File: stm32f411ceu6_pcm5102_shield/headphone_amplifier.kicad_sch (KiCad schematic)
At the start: 17 parts, among them J1 AudioJack3_Ground_SwitchTR, Q1 BC337, Q2 BC337

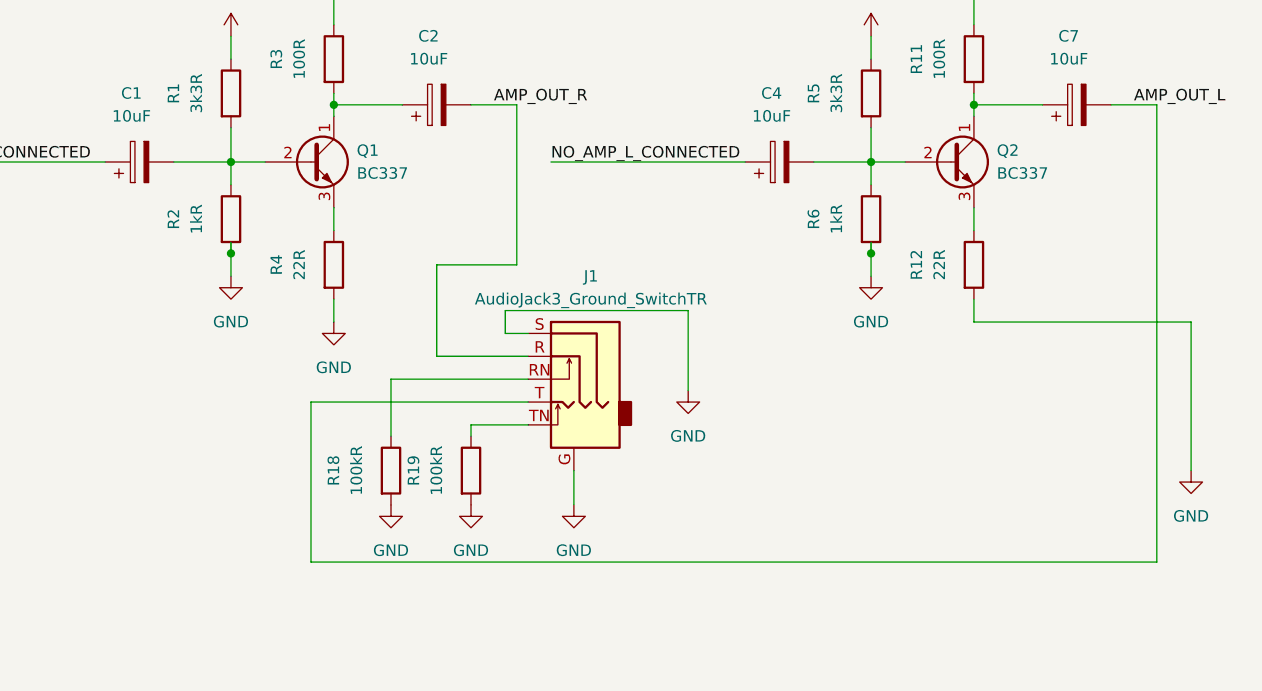
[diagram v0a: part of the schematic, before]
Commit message: Add rotary encoder
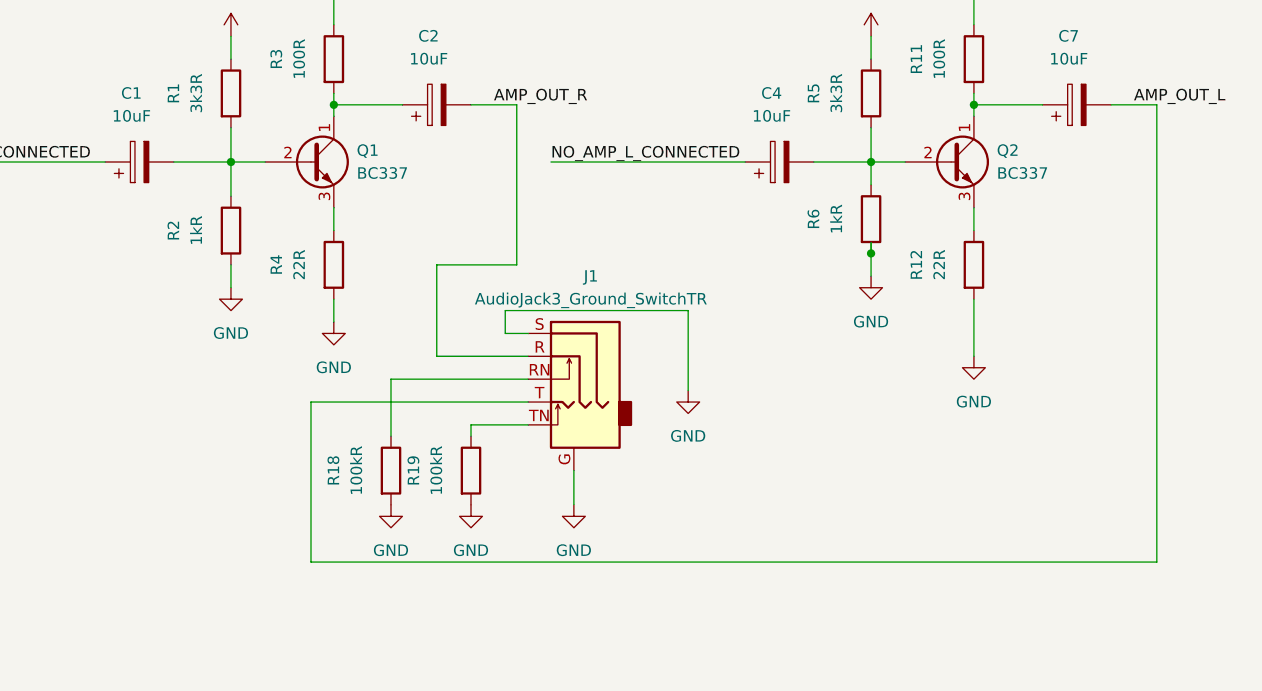
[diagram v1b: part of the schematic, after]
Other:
- moved on the sheet: R2
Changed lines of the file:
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@@
 		(color 0 0 0 0)
 	)
-	(junction
-		(at 59.69 59.69)
-		(diameter 0)
-		(color 0 0 0 0)
-	)
 	(wire
 		(pts
@@
 	(wire
 		(pts
-			(xy 59.69 49.53) (xy 59.69 52.07)
+			(xy 59.69 49.53) (xy 59.69 53.34)
 		)
 		(stroke
@@
 	(wire
 		(pts
-			(xy 142.24 64.77) (xy 142.24 67.31)
-		)
-		(stroke
-			(width 0)
-			(type default)
-		)
-	)
-	(wire
-		(pts
 			(xy 142.24 41.91) (xy 142.24 43.18)
 		)
@@
 	(wire
 		(pts
-			(xy 142.24 67.31) (xy 166.37 67.31)
+			(xy 142.24 43.18) (xy 149.86 43.18)
 		)
 		(stroke
@@
 	(wire
 		(pts
-			(xy 142.24 43.18) (xy 149.86 43.18)
+			(xy 92.71 73.66) (xy 77.47 73.66)
 		)
 		(stroke
@@
 	(wire
 		(pts
-			(xy 92.71 73.66) (xy 77.47 73.66)
+			(xy 124.46 49.53) (xy 130.81 49.53)
 		)
 		(stroke
@@
 	(wire
 		(pts
-			(xy 124.46 49.53) (xy 130.81 49.53)
+			(xy 92.71 78.74) (xy 86.36 78.74)
 		)
 		(stroke
@@
 	(wire
 		(pts
-			(xy 92.71 78.74) (xy 86.36 78.74)
+			(xy 157.48 43.18) (xy 162.56 43.18)
 		)
 		(stroke
@@
 	(wire
 		(pts
-			(xy 157.48 43.18) (xy 162.56 43.18)
+			(xy 59.69 60.96) (xy 59.69 63.5)
 		)
 		(stroke
@@
 	(wire
 		(pts
-			(xy 59.69 59.69) (xy 59.69 62.23)
-		)
-		(stroke
-			(width 0)
-			(type default)
-		)
-	)
-	(wire
-		(pts
-			(xy 166.37 67.31) (xy 166.37 83.82)
+			(xy 142.24 64.77) (xy 142.24 71.12)
 		)
 		(stroke
@@
 	(wire
 		(pts
-			(xy 59.69 58.42) (xy 59.69 59.69)
-		)
-		(stroke
-			(width 0)
-			(type default)
-		)
-	)
-	(wire
-		(pts
 			(xy 130.81 45.72) (xy 130.81 49.53)
 		)
@@
 	(symbol
 		(lib_id "power:GND")
-		(at 59.69 62.23 0)
+		(at 59.69 63.5 0)
 		(unit 1)
 		(exclude_from_sim no)
@@
 		(fields_autoplaced yes)
 		(property "Reference" "#PWR011"
-			(at 59.69 68.58 0)
+			(at 59.69 69.85 0)
 			(effects
 				(font
@@
 		)
 		(property "Value" "GND"
-			(at 59.69 67.31 0)
+			(at 59.69 68.58 0)
 			(effects
 				(font
@@
 		)
 		(property "Footprint" ""
-			(at 59.69 62.23 0)
+			(at 59.69 63.5 0)
 			(effects
 				(font
@@
 		)
 		(property "Datasheet" ""
-			(at 59.69 62.23 0)
+			(at 59.69 63.5 0)
 			(effects
 				(font
@@
 		)
 		(property "Description" "Power symbol creates a global label with name \"GND\" , ground"
-			(at 59.69 62.23 0)
+			(at 59.69 63.5 0)
 			(effects
 				(font
@@
 	(symbol
 		(lib_id "Device:R")
-		(at 59.69 55.88 0)
+		(at 59.69 57.15 0)
 		(unit 1)
 		(exclude_from_sim no)
@@
 		(dnp no)
 		(property "Reference" "R2"
-			(at 53.34 55.88 90)
+			(at 53.34 57.15 90)
 			(effects
 				(font
@@
 		)
 		(property "Value" "1kR"
-			(at 55.88 55.88 90)
+			(at 55.88 57.15 90)
 			(effects
 				(font
@@
 		)
 		(property "Footprint" "Resistor_SMD:R_0805_2012Metric"
-			(at 57.912 55.88 90)
+			(at 57.912 57.15 90)
 			(effects
 				(font
@@
 		)
 		(property "Datasheet" "~"
-			(at 59.69 55.88 0)
+			(at 59.69 57.15 0)
 			(effects
 				(font
@@
 		)
 		(property "Description" ""
-			(at 59.69 55.88 0)
+			(at 59.69 57.15 0)
 			(effects
 				(font
@@
 		)
 		(property "LCSC link" "https://www.lcsc.com/product-detail/Chip-Resistor-Surface-Mount_UNI-ROYAL-Uniroyal-Elec-0805W8F100JT5E_C17415.html"
-			(at 59.69 55.88 0)
+			(at 59.69 57.15 0)
 			(effects
 				(font
@@
 		)
 		(property "Manufacturer" "UNI-ROYAL(Uniroyal Elec)"
-			(at 59.69 55.88 0)
+			(at 59.69 57.15 0)
 			(effects
 				(font
@@
 		)
 		(property "Manufacturer Part Number" "0805W8F100JT5E"
-			(at 59.69 55.88 0)
+			(at 59.69 57.15 0)
 			(effects
 				(font
@@
 	(symbol
 		(lib_id "power:GND")
-		(at 166.37 83.82 0)
+		(at 142.24 71.12 0)
 		(unit 1)
 		(exclude_from_sim no)
@@
 		(fields_autoplaced yes)
 		(property "Reference" "#PWR023"
-			(at 166.37 90.17 0)
+			(at 142.24 77.47 0)
 			(effects
 				(font
@@
 		)
 		(property "Value" "GND"
-			(at 166.37 88.9 0)
+			(at 142.24 76.2 0)
 			(effects
 				(font
@@
 		)
 		(property "Footprint" ""
-			(at 166.37 83.82 0)
+			(at 142.24 71.12 0)
 			(effects
 				(font
@@
 		)
 		(property "Datasheet" ""
-			(at 166.37 83.82 0)
+			(at 142.24 71.12 0)
 			(effects
 				(font
@@
 		)
 		(property "Description" "Power symbol creates a global label with name \"GND\" , ground"
-			(at 166.37 83.82 0)
+			(at 142.24 71.12 0)
 			(effects
 				(font

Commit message: Items numeration fix
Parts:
- renumbered C1 to C300, C2 to C301, C4 to C302, C7 to C303, J1 to J300, Q1 to Q300, Q2 to Q301, R1 to R300, R2 to R301, R3 to R302, R4 to R303, R5 to R304, R6 to R305, R11 to R306, R12 to R307, R18 to R308, R19 to R309
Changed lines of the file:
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@@
 		(dnp no)
 		(fields_autoplaced yes)
-		(property "Reference" "C1"
+		(property "Reference" "C300"
 			(at 48.641 41.91 90)
 			(effects
@@
 			(project "stm32f411ceu6_pcm5102_shield"
 				(path "/aeaad843-2b7c-40e9-bb1d-8d1f5e5d5206/73f0023b-2db5-4e36-9906-e9384dd08abf"
-					(reference "C1")
+					(reference "C300")
 					(unit 1)
 				)
@@
 		(dnp no)
 		(fields_autoplaced yes)
-		(property "Reference" "C2"
+		(property "Reference" "C301"
 			(at 81.661 35.56 90)
 			(effects
@@
 			(project "stm32f411ceu6_pcm5102_shield"
 				(path "/aeaad843-2b7c-40e9-bb1d-8d1f5e5d5206/73f0023b-2db5-4e36-9906-e9384dd08abf"
-					(reference "C2")
+					(reference "C301")
 					(unit 1)
 				)
@@
 		(on_board yes)
 		(dnp no)
-		(property "Reference" "R11"
+		(property "Reference" "R306"
 			(at 135.89 38.1 90)
 			(effects
@@
 			(project "stm32f411ceu6_pcm5102_shield"
 				(path "/aeaad843-2b7c-40e9-bb1d-8d1f5e5d5206/73f0023b-2db5-4e36-9906-e9384dd08abf"
-					(reference "R11")
+					(reference "R306")
 					(unit 1)
 				)
@@
 		(dnp no)
 		(fields_autoplaced yes)
-		(property "Reference" "C7"
+		(property "Reference" "C303"
 			(at 152.781 35.56 90)
 			(effects
@@
 			(project "stm32f411ceu6_pcm5102_shield"
 				(path "/aeaad843-2b7c-40e9-bb1d-8d1f5e5d5206/73f0023b-2db5-4e36-9906-e9384dd08abf"
-					(reference "C7")
+					(reference "C303")
 					(unit 1)
 				)
@@
 		(on_board yes)
 		(dnp no)
-		(property "Reference" "R19"
+		(property "Reference" "R309"
 			(at 80.01 83.82 90)
 			(effects
@@
 			(project "stm32f411ceu6_pcm5102_shield"
 				(path "/aeaad843-2b7c-40e9-bb1d-8d1f5e5d5206/73f0023b-2db5-4e36-9906-e9384dd08abf"
-					(reference "R19")
+					(reference "R309")
 					(unit 1)
 				)
@@
 		(on_board yes)
 		(dnp no)
-		(property "Reference" "R18"
+		(property "Reference" "R308"
 			(at 71.12 83.82 90)
 			(effects
@@
 			(project "stm32f411ceu6_pcm5102_shield"
 				(path "/aeaad843-2b7c-40e9-bb1d-8d1f5e5d5206/73f0023b-2db5-4e36-9906-e9384dd08abf"
-					(reference "R18")
+					(reference "R308")
 					(unit 1)
 				)
@@
 		(dnp no)
 		(fields_autoplaced yes)
-		(property "Reference" "C4"
+		(property "Reference" "C302"
 			(at 119.761 41.91 90)
 			(effects
@@
 			(project "stm32f411ceu6_pcm5102_shield"
 				(path "/aeaad843-2b7c-40e9-bb1d-8d1f5e5d5206/73f0023b-2db5-4e36-9906-e9384dd08abf"
-					(reference "C4")
+					(reference "C302")
 					(unit 1)
 				)
@@
 		(on_board yes)
 		(dnp no)
-		(property "Reference" "R2"
+		(property "Reference" "R301"
 			(at 53.34 57.15 90)
 			(effects
@@
 			(project "stm32f411ceu6_pcm5102_shield"
 				(path "/aeaad843-2b7c-40e9-bb1d-8d1f5e5d5206/73f0023b-2db5-4e36-9906-e9384dd08abf"
-					(reference "R2")
+					(reference "R301")
 					(unit 1)
 				)
@@
 		(dnp no)
 		(fields_autoplaced yes)
-		(property "Reference" "Q2"
+		(property "Reference" "Q301"
 			(at 144.78 48.2599 0)
 			(effects
@@
 			(project "stm32f411ceu6_pcm5102_shield"
 				(path "/aeaad843-2b7c-40e9-bb1d-8d1f5e5d5206/73f0023b-2db5-4e36-9906-e9384dd08abf"
-					(reference "Q2")
+					(reference "Q301")
 					(unit 1)
 				)
@@
 		(on_board yes)
 		(dnp no)
-		(property "Reference" "R12"
+		(property "Reference" "R307"
 			(at 135.89 60.96 90)
 			(effects
@@
 			(project "stm32f411ceu6_pcm5102_shield"
 				(path "/aeaad843-2b7c-40e9-bb1d-8d1f5e5d5206/73f0023b-2db5-4e36-9906-e9384dd08abf"
-					(reference "R12")
+					(reference "R307")
 					(unit 1)
 				)
@@
 		(dnp no)
 		(fields_autoplaced yes)
-		(property "Reference" "J1"
+		(property "Reference" "J300"
 			(at 99.695 62.23 0)
 			(effects
@@
 			(project "stm32f411ceu6_pcm5102_shield"
 				(path "/aeaad843-2b7c-40e9-bb1d-8d1f5e5d5206/73f0023b-2db5-4e36-9906-e9384dd08abf"
-					(reference "J1")
+					(reference "J300")
 					(unit 1)
 				)
@@
 		(on_board yes)
 		(dnp no)
-		(property "Reference" "R5"
+		(property "Reference" "R304"
 			(at 124.46 41.91 90)
 			(effects
@@
 			(project "stm32f411ceu6_pcm5102_shield"
 				(path "/aeaad843-2b7c-40e9-bb1d-8d1f5e5d5206/73f0023b-2db5-4e36-9906-e9384dd08abf"
-					(reference "R5")
+					(reference "R304")
 					(unit 1)
 				)
@@
 		(on_board yes)
 		(dnp no)
-		(property "Reference" "R4"
+		(property "Reference" "R303"
 			(at 64.77 60.96 90)
 			(effects
@@
 			(project "stm32f411ceu6_pcm5102_shield"
 				(path "/aeaad843-2b7c-40e9-bb1d-8d1f5e5d5206/73f0023b-2db5-4e36-9906-e9384dd08abf"
-					(reference "R4")
+					(reference "R303")
 					(unit 1)
 				)
@@
 		(on_board yes)
 		(dnp no)
-		(property "Reference" "R1"
+		(property "Reference" "R300"
 			(at 53.34 41.91 90)
 			(effects
@@
 			(project "stm32f411ceu6_pcm5102_shield"
 				(path "/aeaad843-2b7c-40e9-bb1d-8d1f5e5d5206/73f0023b-2db5-4e36-9906-e9384dd08abf"
-					(reference "R1")
+					(reference "R300")
 					(unit 1)
 				)
@@
 		(on_board yes)
 		(dnp no)
-		(property "Reference" "R3"
+		(property "Reference" "R302"
 			(at 64.77 38.1 90)
 			(effects
@@
 			(project "stm32f411ceu6_pcm5102_shield"
 				(path "/aeaad843-2b7c-40e9-bb1d-8d1f5e5d5206/73f0023b-2db5-4e36-9906-e9384dd08abf"
-					(reference "R3")
+					(reference "R302")
 					(unit 1)
 				)
@@
 		(dnp no)
 		(fields_autoplaced yes)
-		(property "Reference" "Q1"
+		(property "Reference" "Q300"
 			(at 73.66 48.2599 0)
 			(effects
@@
 			(project "stm32f411ceu6_pcm5102_shield"
 				(path "/aeaad843-2b7c-40e9-bb1d-8d1f5e5d5206/73f0023b-2db5-4e36-9906-e9384dd08abf"
-					(reference "Q1")
+					(reference "Q300")
 					(unit 1)
 				)
@@
 		(on_board yes)
 		(dnp no)
-		(property "Reference" "R6"
+		(property "Reference" "R305"
 			(at 124.46 55.88 90)
 			(effects
@@
 			(project "stm32f411ceu6_pcm5102_shield"
 				(path "/aeaad843-2b7c-40e9-bb1d-8d1f5e5d5206/73f0023b-2db5-4e36-9906-e9384dd08abf"
-					(reference "R6")
-					(unit 1)
-				)
+					(reference "R305")
+					(unit 1)
+				)

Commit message: BOM updates
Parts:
- added R310, R311: 100kR, Resistor_SMD:R_0805_2012Metric, symbol Device:R
- C300, C301, C302, C303: footprint (none) -> Capacitor_Tantalum_SMD:CP_EIA-3216-18_Kemet-A; Manufacturer (none) -> Kyocera AVX; Manufacturer Part Number (none) -> TAJA106K016RNJ
- R300, R304: Manufacturer Part Number 0805W8F100JT5E -> 0805W8F3301T5E
- R301, R305: Manufacturer Part Number 0805W8F100JT5E -> 0805W8F1001T5E
- R302, R306: Manufacturer Part Number 0805W8F100JT5E -> 0805W8F1000T5E
- R303, R307: Manufacturer Part Number 0805W8F100JT5E -> 0805W8F220JT5E
- R308, R309: Manufacturer Part Number 0805W8F100JT5E -> 0805W8J0104T5E
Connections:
- net GND: now also R310.1, R311.1
- net NO_AMP_L_CONNECTED: now also R311.2
- net NO_AMP_R_CONNECTED: now also R310.2
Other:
- moved on the sheet: C302, C303, Q301, R304, R305, R306, R307

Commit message: Put all items on a board
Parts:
- J300: footprint Connector_Audio:Jack_3.5mm_PJ311_Horizontal -> stm32f401_pcm5102_shiled_lib:AudioJack_3.5mm_PJ311
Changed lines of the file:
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@@
 			)
 		)
-		(property "Footprint" "Connector_Audio:Jack_3.5mm_PJ311_Horizontal"
+		(property "Footprint" "stm32f401_pcm5102_shiled_lib:AudioJack_3.5mm_PJ311"
 			(at 97.79 71.12 0)
 			(effects

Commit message: PCB rules setup
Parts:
- added J301: Conn_01x03_Pin, Connector_PinHeader_2.54mm:PinHeader_1x03_P2.54mm_Vertical, symbol Connector:Conn_01x03_Pin
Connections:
- net AMP_OUT_L: now also J301.2 (Pin_2)
- net AMP_OUT_R: now also J301.3 (Pin_3)
- net GND: now also J301.1 (Pin_1)
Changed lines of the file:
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@@
 	)
 	(junction
+		(at 91.44 58.42)
+		(diameter 0)
+		(color 0 0 0 0)
+	)
+	(junction
 		(at 170.18 46.99)
 		(diameter 0)
@@
 	)
 	(junction
+		(at 118.11 93.98)
+		(diameter 0)
+		(color 0 0 0 0)
+	)
+	(junction
 		(at 71.12 43.18)
 		(diameter 0)
@@
 	(wire
 		(pts
+			(xy 91.44 58.42) (xy 118.11 58.42)
+		)
+		(stroke
+			(width 0)
+			(type default)
+		)
+	)
+	(wire
+		(pts
 			(xy 59.69 49.53) (xy 59.69 53.34)
 		)
@@
 	(wire
 		(pts
-			(xy 91.44 43.18) (xy 91.44 60.96)
+			(xy 91.44 43.18) (xy 91.44 58.42)
 		)
 		(stroke
@@
 	(wire
 		(pts
+			(xy 118.11 58.42) (xy 118.11 72.39)
+		)
+		(stroke
+			(width 0)
+			(type default)
+		)
+	)
+	(wire
+		(pts
 			(xy 90.17 66.04) (xy 110.49 66.04)
 		)
@@
 	(wire
 		(pts
+			(xy 91.44 58.42) (xy 91.44 60.96)
+		)
+		(stroke
+			(width 0)
+			(type default)
+		)
+	)
+	(wire
+		(pts
 			(xy 181.61 39.37) (xy 181.61 40.64)
 		)
@@
 	(wire
 		(pts
+			(xy 118.11 74.93) (xy 125.73 74.93)
+		)
+		(stroke
+			(width 0)
+			(type default)
+		)
+	)
+	(wire
+		(pts
 			(xy 181.61 40.64) (xy 189.23 40.64)
 		)
@@
 	(wire
 		(pts
+			(xy 125.73 77.47) (xy 125.73 81.28)
+		)
+		(stroke
+			(width 0)
+			(type default)
+		)
+	)
+	(wire
+		(pts
+			(xy 118.11 72.39) (xy 125.73 72.39)
+		)
+		(stroke
+			(width 0)
+			(type default)
+		)
+	)
+	(wire
+		(pts
 			(xy 92.71 78.74) (xy 86.36 78.74)
 		)
@@
 	(wire
 		(pts
+			(xy 118.11 93.98) (xy 68.58 93.98)
+		)
+		(stroke
+			(width 0)
+			(type default)
+		)
+	)
+	(wire
+		(pts
 			(xy 170.18 43.18) (xy 170.18 46.99)
 		)
@@
 	(wire
 		(pts
-			(xy 201.93 93.98) (xy 68.58 93.98)
+			(xy 201.93 93.98) (xy 118.11 93.98)
+		)
+		(stroke
+			(width 0)
+			(type default)
+		)
+	)
+	(wire
+		(pts
+			(xy 118.11 93.98) (xy 118.11 74.93)
 		)
 		(stroke
@@
 	)
 	(symbol
+		(lib_id "Connector:Conn_01x03_Pin")
+		(at 130.81 74.93 180)
+		(unit 1)
+		(exclude_from_sim no)
+		(in_bom yes)
+		(on_board yes)
+		(dnp no)
+		(fields_autoplaced yes)
+		(property "Reference" "J301"
+			(at 132.08 73.6599 0)
+			(effects
+				(font
+					(size 1.27 1.27)
+				)
+				(justify right)
+			)
+		)
+		(property "Value" "Conn_01x03_Pin"
+			(at 132.08 76.1999 0)
+			(effects
+				(font
+					(size 1.27 1.27)
+				)
+				(justify right)
+			)
+		)
+		(property "Footprint" "Connector_PinHeader_2.54mm:PinHeader_1x03_P2.54mm_Vertical"
+			(at 130.81 74.93 0)
+			(effects
+				(font
+					(size 1.27 1.27)
+				)
+				(hide yes)
+			)
+		)
+		(property "Datasheet" "~"
+			(at 130.81 74.93 0)
+			(effects
+				(font
+					(size 1.27 1.27)
+				)
+				(hide yes)
+			)
+		)
+		(property "Description" "Generic connector, single row, 01x03, script generated"
+			(at 130.81 74.93 0)
+			(effects
+				(font
+					(size 1.27 1.27)
+				)
+				(hide yes)
+			)
+		)
+		(pin "2"
+		)
+		(pin "3"
+		)
+		(pin "1"
+		)
+		(instances
+			(project "stm32f411ceu6_pcm5102_shield"
+				(path "/aeaad843-2b7c-40e9-bb1d-8d1f5e5d5206/73f0023b-2db5-4e36-9906-e9384dd08abf"
+					(reference "J301")
+					(unit 1)
+				)
+			)
+		)
+	)
+	(symbol
 		(lib_id "Device:C_Polarized")
 		(at 193.04 40.64 90)
@@
 					(unit 1)
 				)
+			)
+		)
+	)
+	(symbol
+		(lib_id "power:GND")
+		(at 125.73 81.28 0)
+		(mirror y)
+		(unit 1)
+		(exclude_from_sim no)
+		(in_bom yes)
+		(on_board yes)
+		(dnp no)
+		(fields_autoplaced yes)
+		(property "Reference" "#PWR069"
+			(at 125.73 87.63 0)
+			(effects
+				(font
+					(size 1.27 1.27)
+				)
+				(hide yes)
+			)
+		)
+		(property "Value" "GND"
+			(at 125.73 86.36 0)
+			(effects
+				(font
+					(size 1.27 1.27)
+				)
+			)
+		)
+		(property "Footprint" ""
+			(at 125.73 81.28 0)
+			(effects
+				(font
+					(size 1.27 1.27)
+				)
+				(hide yes)
+			)
+		)
+		(property "Datasheet" ""
+			(at 125.73 81.28 0)
+			(effects
+				(font
+					(size 1.27 1.27)
+				)
+				(hide yes)
+			)
+		)
+		(property "Description" "Power symbol creates a global label with name \"GND\" , ground"
+			(at 125.73 81.28 0)
+			(effects
+				(font
+					(size 1.27 1.27)
+				)
+				(hide yes)
+			)
+		)
+		(pin "1"
+		)
+		(instances
+			(project "stm32f411ceu6_pcm5102_shield"
+				(path "/aeaad843-2b7c-40e9-bb1d-8d1f5e5d5206/73f0023b-2db5-4e36-9906-e9384dd08abf"
+					(reference "#PWR069")
+					(unit 1)
+				)

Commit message: Initial layout
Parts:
- Q300, Q301: Manufacturer (none) -> LGE; Manufacturer Part Number (none) -> LGE BC337-40
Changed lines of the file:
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@@
+			)
+		)
+		(property "Manufacturer" "LGE"
+			(at 179.07 46.99 0)
+			(effects
+				(font
+					(size 1.27 1.27)
+				)
+				(hide yes)
+			)
+		)
+		(property "Manufacturer Part Number" "LGE BC337-40"
+			(at 179.07 46.99 0)
+			(effects
+				(font
+					(size 1.27 1.27)
+				)
+				(hide yes)
 			)
 		)
@@
 			(at 68.58 49.53 0)
 			(effects
+				(font
+					(size 1.27 1.27)
+				)
+				(hide yes)
+			)
+		)
+		(property "Manufacturer" "LGE"
+			(at 68.58 49.53 0)
+			(effects
+				(font
+					(size 1.27 1.27)
+				)
+				(hide yes)
+			)
+		)
+		(property "Manufacturer Part Number" "LGE BC337-40"
+			(at 68.58 49.53 0)
+			(effects

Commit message: BOM fixes
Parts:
- R303, R307: footprint Resistor_SMD:R_0805_2012Metric -> Resistor_SMD:R_0603_1608Metric; Manufacturer Part Number 0805W8F220JT5E -> 0603WAF220JT5E
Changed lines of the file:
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@@
 			)
 		)
-		(property "Footprint" "Resistor_SMD:R_0805_2012Metric"
+		(property "Footprint" "Resistor_SMD:R_0603_1608Metric"
 			(at 179.832 58.42 90)
 			(effects
@@
 			)
 		)
-		(property "Manufacturer Part Number" "0805W8F220JT5E"
+		(property "Manufacturer Part Number" "0603WAF220JT5E"
 			(at 181.61 58.42 0)
 			(effects
@@
 			)
 		)
-		(property "Footprint" "Resistor_SMD:R_0805_2012Metric"
+		(property "Footprint" "Resistor_SMD:R_0603_1608Metric"
 			(at 69.342 60.96 90)
 			(effects
@@
 			)
 		)
-		(property "Manufacturer Part Number" "0805W8F220JT5E"
+		(property "Manufacturer Part Number" "0603WAF220JT5E"
 			(at 71.12 60.96 0)
 			(effects
